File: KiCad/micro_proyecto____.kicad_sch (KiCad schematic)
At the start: 37 parts, among them J1 Conn_01x02, J2 Conn_01x05, J3 Conn_01x02, J4 Conn_01x02, J5 Conn_01x02, J6 Conn_01x02, SW1 SW_Push, SW2 SW_Push, SW3 SW_Push, SW4 SW_Push, SW5 SW_Push, SW6 SW_Push, U4 PIC24HJ128GP502, Y1 Crystal

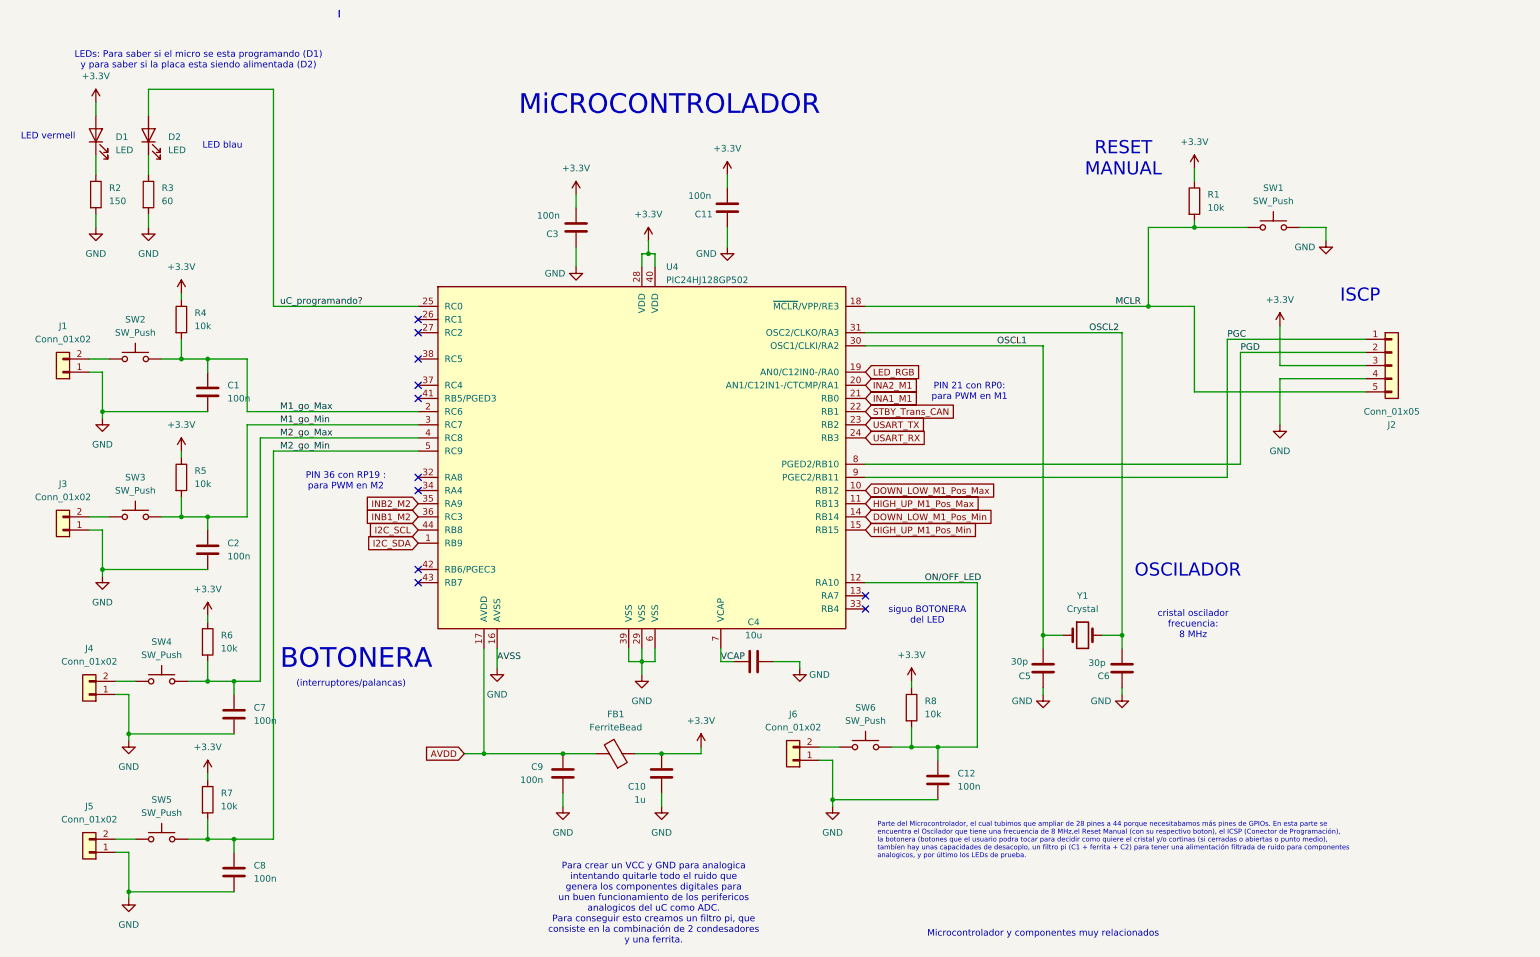
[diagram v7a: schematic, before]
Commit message: pujo el esquematico a medio hacer despues de hacer cambios para mejorar el 2o layout
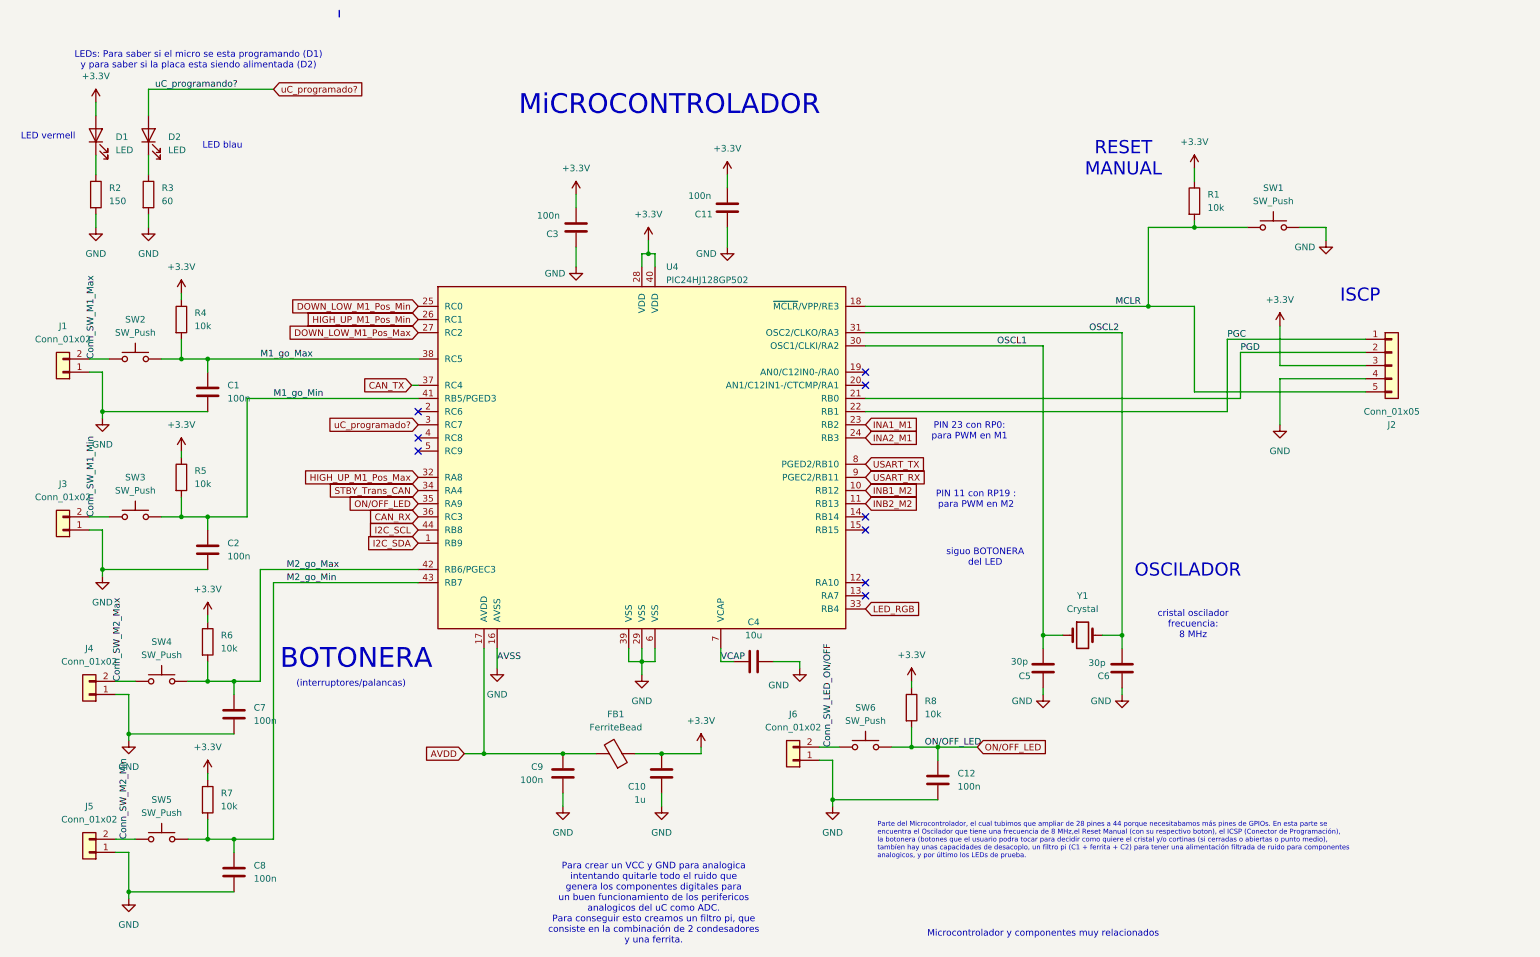
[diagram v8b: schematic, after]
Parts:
- J1, J3, J4, J5, J6: footprint Connector_PinHeader_2.54mm:PinHeader_1x02_P2.54mm_Horizontal -> Connector_PinHeader_2.54mm:PinHeader_1x02_P2.54mm_Vertical
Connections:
- net DOWN_LOW_M1_Pos_Max: now also U4.27 (RC2); no longer U4.10 (RB12)
- net DOWN_LOW_M1_Pos_Min: now also U4.25 (RC0); no longer U4.14 (RB14)
- net HIGH_UP_M1_Pos_Max: now also U4.32 (RA8); no longer U4.11 (RB13)
- net HIGH_UP_M1_Pos_Min: now also U4.26 (RC1); no longer U4.15 (RB15)
- net INA1_M1: now also U4.23 (RB2); no longer U4.21 (RB0)
- net INA2_M1: now also U4.24 (RB3); no longer U4.20 (AN1/C12IN1-/CTCMP/RA1)
- net INB1_M2: now also U4.10 (RB12); no longer U4.36 (RC3)
- net INB2_M2: now also U4.11 (RB13); no longer U4.35 (RA9)
- net LED_RGB: now also U4.33 (RB4); no longer U4.19 (AN0/C12IN0-/RA0)
- net M1_go_Max: now also U4.38 (RC5); no longer U4.2 (RC6)
- net M1_go_Min: now also U4.41 (RB5/PGED3); no longer U4.3 (RC7)
- net M2_go_Max: now also U4.42 (RB6/PGEC3); no longer U4.4 (RC8)
- net M2_go_Min: now also U4.43 (RB7); no longer U4.5 (RC9)
- net ON/OFF_LED: now also U4.35 (RA9); no longer U4.12 (RA10)
- net PGC: now also U4.22 (RB1); no longer U4.9 (PGEC2/RB11)
- net PGD: now also U4.21 (RB0); no longer U4.8 (PGED2/RB10)
- net STBY_Trans_CAN: now also U4.34 (NC); no longer U4.22 (RB1)
- net USART_RX: now also U4.9 (PGEC2/RB11); no longer U4.24 (RB3)
- net USART_TX: now also U4.8 (PGED2/RB10); no longer U4.23 (RB2)
- net Conn_SW_M2_Min: now reaches J5.2 (Pin_2), SW5.1
- net Conn_SW_M2_Max: now reaches J4.2 (Pin_2), SW4.1
- net Conn_SW_LED_ON/OFF: now reaches J6.2 (Pin_2), SW6.1
- net Conn_SW_M1_Max: now reaches J1.2 (Pin_2), SW2.1
- net Conn_SW_M1_Min: now reaches J3.2 (Pin_2), SW3.1
- net CAN_TX: now reaches U4.37 (RC4)
- net uC_programando? renamed uC_programado?
- net uC_programado?: now also U4.3 (RC7); no longer U4.25 (RC0)
- new net CAN_RX: U4.36 (RC3)
- no-connect marks 11 -> 9
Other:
- note added: "PIN 11 con RP19 : para PWM en M2"
- note added: "PIN 23 con RP0: para PWM en M1"
- note removed: "PIN 21 con RP0: para PWM en M1"
- note removed: "PIN 36 con RP19 : para PWM en M2"
